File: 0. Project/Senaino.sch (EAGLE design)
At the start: 34 parts, among them Q1 16 MHz, U1 ATMEGA328P-PU, U2 FT232RL, U3 7805T, X1 POWERSUPPLY_DC21MMX

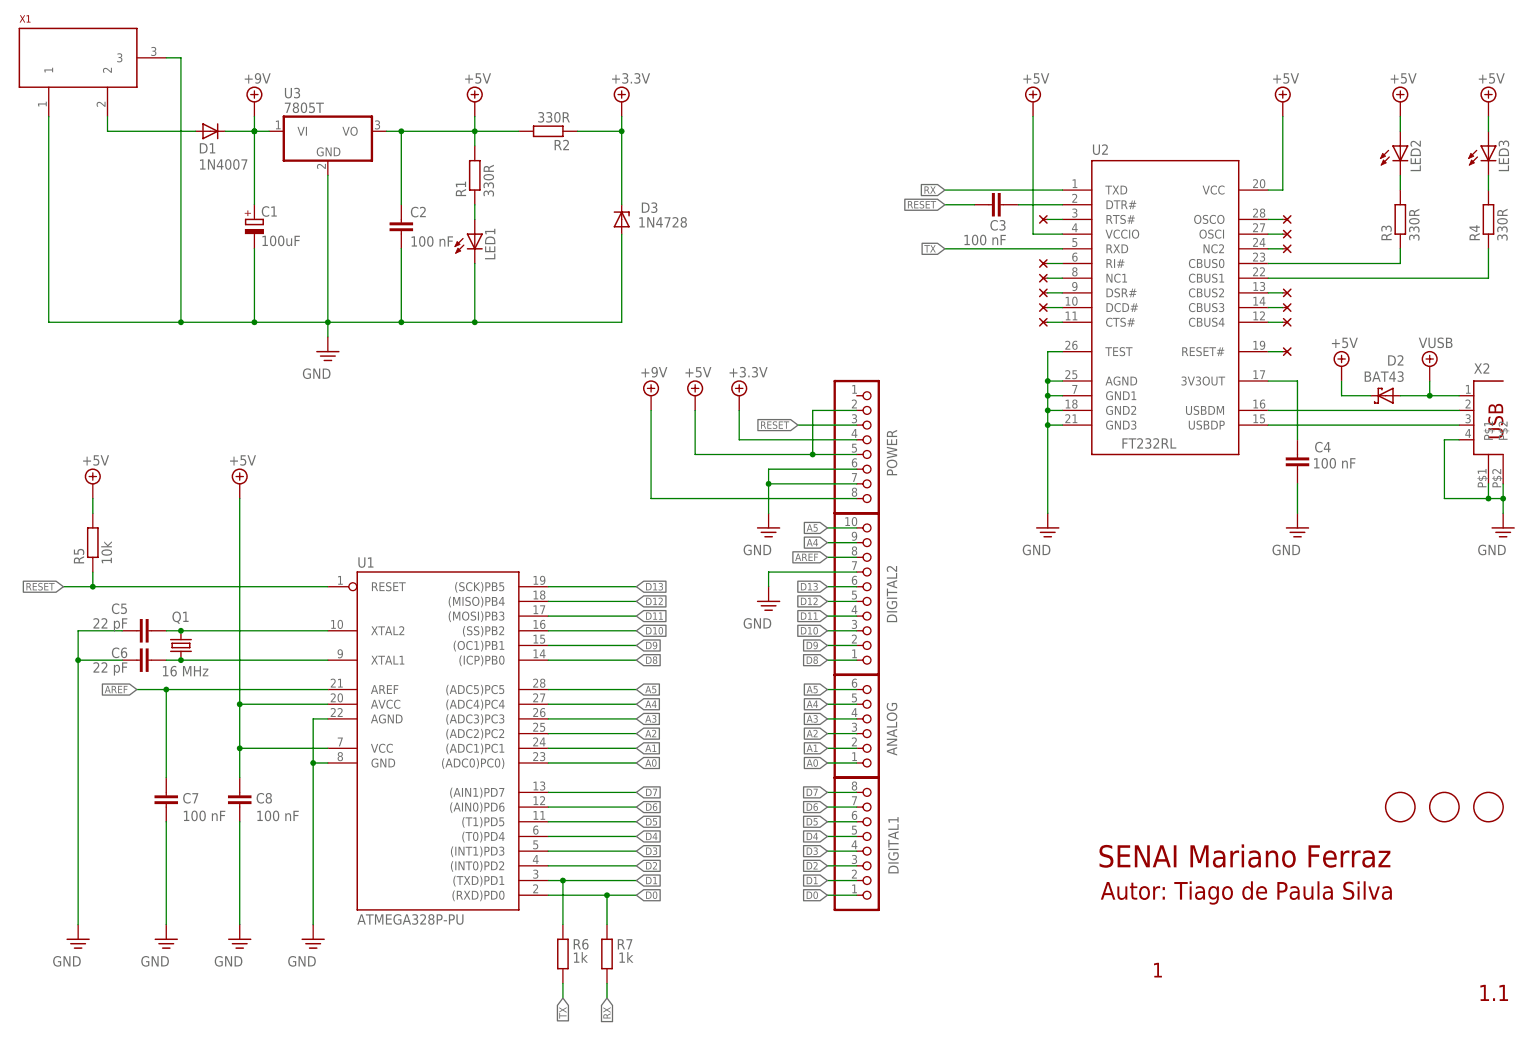
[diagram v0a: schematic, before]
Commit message: Frame schematic updated
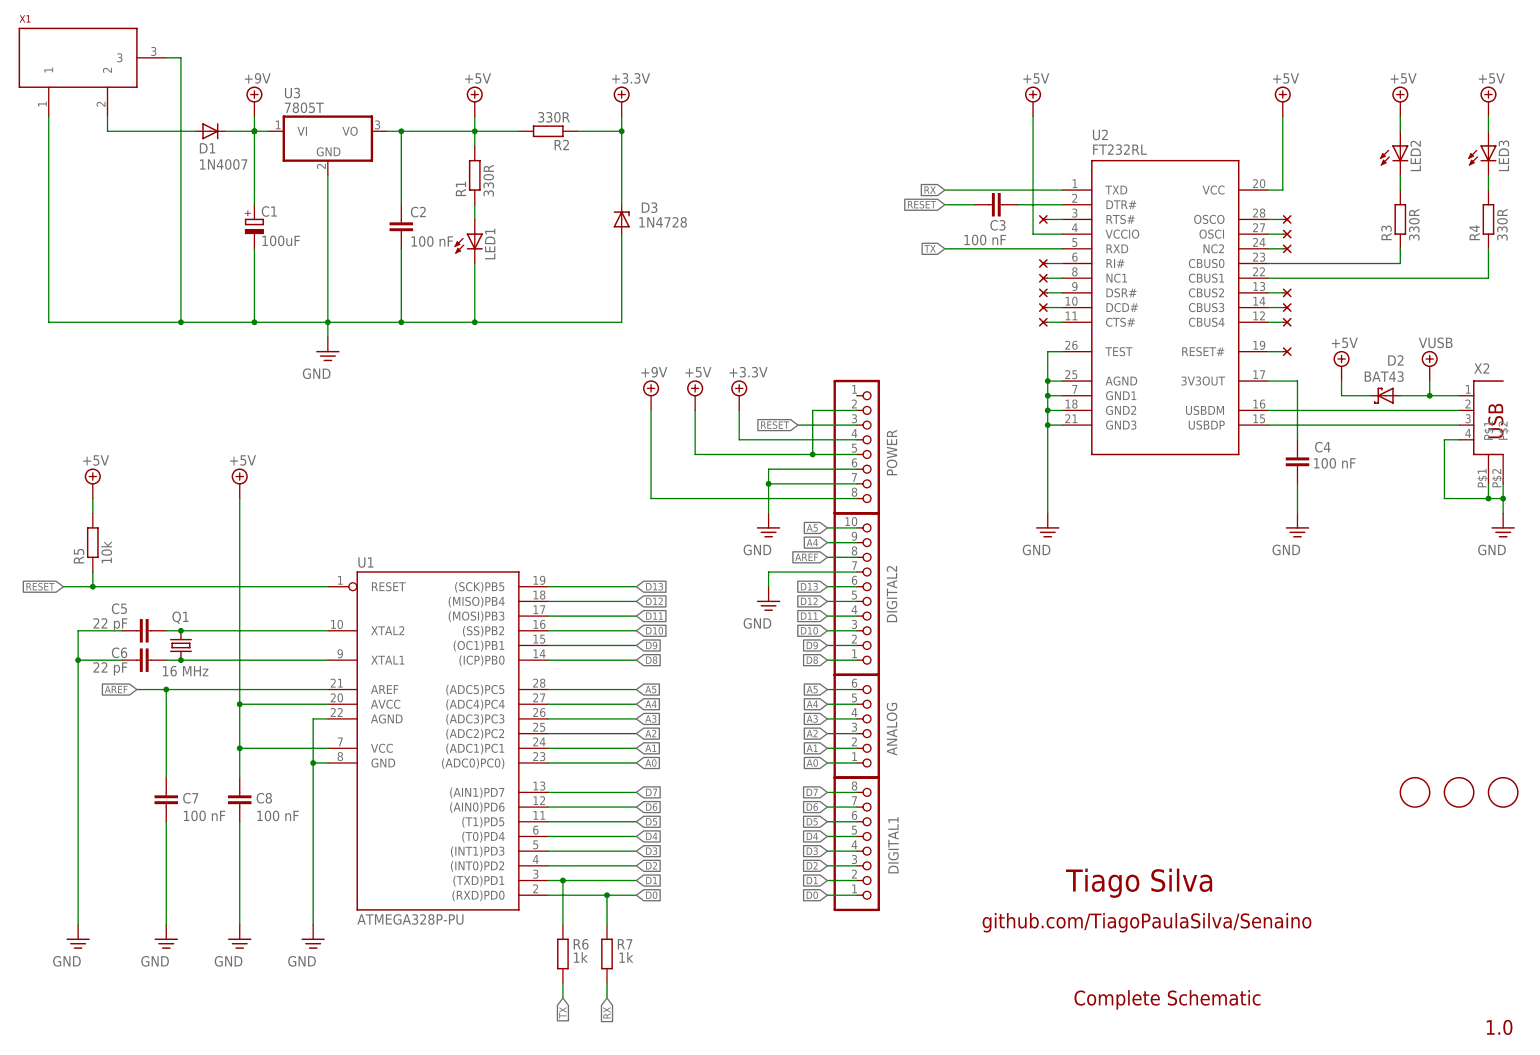
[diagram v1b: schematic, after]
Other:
- note added: "1.0"
- note added: "Complete Schematic"
- note added: "Tiago Silva"
- note added: "github.com/TiagoPaulaSilva/Senaino"
- note removed: "1"
- note removed: "1.1"
- note removed: "Autor: Tiago de Paula Silva"
- note removed: "SENAI Mariano Ferraz"
